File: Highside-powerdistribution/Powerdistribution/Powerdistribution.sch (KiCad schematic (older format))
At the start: 9 parts, among them J1 Screw_Terminal_01x02, J2 Screw_Terminal_01x02, J3 Screw_Terminal_01x02, J4 Screw_Terminal_01x02, J5 Screw_Terminal_01x02, J6 Screw_Terminal_01x02, J7 Screw_Terminal_01x02, J8 Screw_Terminal_01x02, J9 Screw_Terminal_01x02

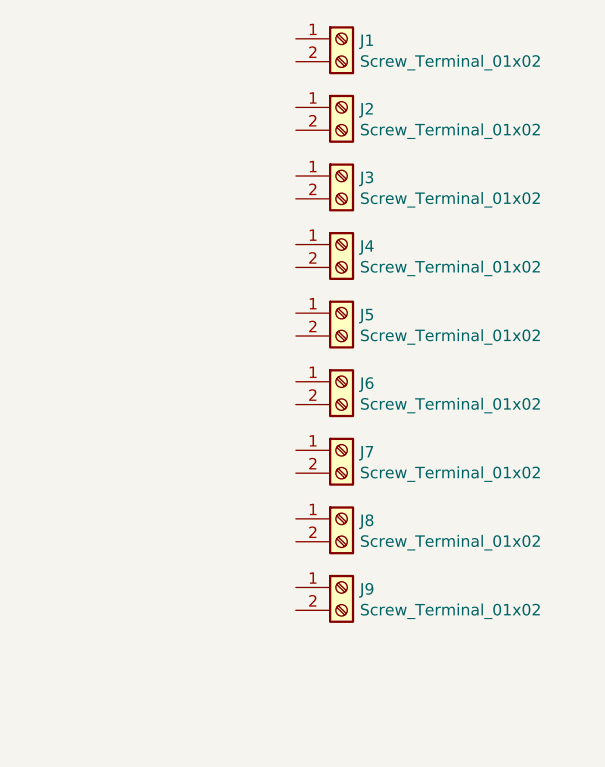
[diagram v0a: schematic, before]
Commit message: Moved filled zone to remove shortcurcit
12V and the mosfets had filled zone together
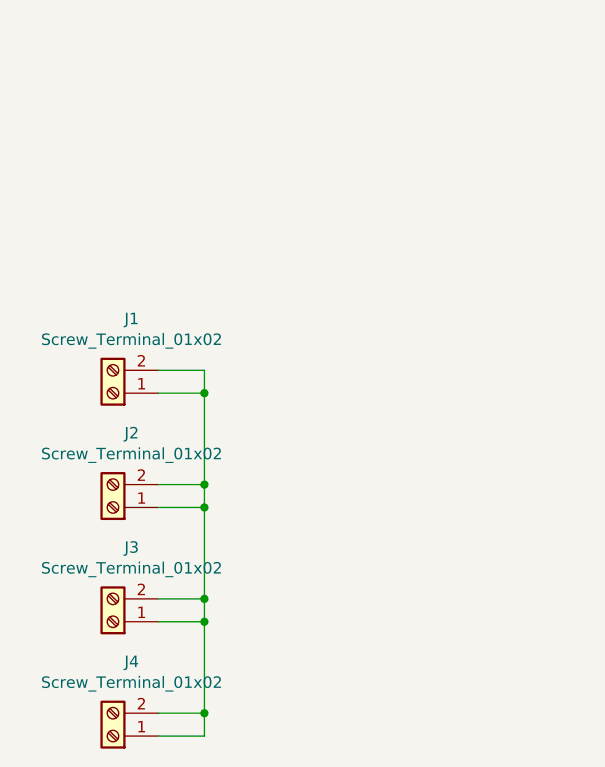
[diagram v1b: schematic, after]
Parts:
- removed J5, J6, J7, J8, J9: Screw_Terminal_01x02, TerminalBlock_TE-Connectivity:TerminalBlock_TE_282834-2_1x02_P2.54mm_Horizontal, symbol Connector:Screw_Terminal_01x02
- J1, J2, J3, J4: footprint TerminalBlock_TE-Connectivity:TerminalBlock_TE_282834-2_1x02_P2.54mm_Horizontal -> Highside-powerdistribution:Phoenix_TB_2-1935776
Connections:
- net at J1.1 (Pin_1): now also J1.2 (Pin_2), J2.1 (Pin_1), J2.2 (Pin_2), J3.1 (Pin_1), J3.2 (Pin_2), J4.1 (Pin_1), J4.2 (Pin_2)
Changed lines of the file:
@@
 EESchema Schematic File Version 4
+LIBS:Powerdistribution-cache
 EELAYER 30 0
 EELAYER END
@@
 $Comp
 L Connector:Screw_Terminal_01x02 J1
-U 1 1 5DD2F273
-P 6000 2000
-F 0 "J1" H 6080 1992 50  0000 L CNN
-F 1 "Screw_Terminal_01x02" H 6080 1901 50  0000 L CNN
-F 2 "TerminalBlock_TE-Connectivity:TerminalBlock_TE_282834-2_1x02_P2.54mm_Horizontal" H 6000 2000 50  0001 C CNN
-F 3 "~" H 6000 2000 50  0001 C CNN
-	1    6000 2000
-	1    0    0    -1
+U 1 1 5DDAC855
+P 5000 3550
+F 0 "J1" H 4918 3225 50  0000 C CNN
+F 1 "Screw_Terminal_01x02" H 4918 3316 50  0000 C CNN
+F 2 "Highside-powerdistribution:Phoenix_TB_2-1935776" H 5000 3550 50  0001 C CNN
+F 3 "~" H 5000 3550 50  0001 C CNN
+	1    5000 3550
+	-1   0    0    1
 $EndComp
+Wire Wire Line
+	5200 3450 5400 3450
 $Comp
 L Connector:Screw_Terminal_01x02 J2
-U 1 1 5DD30E21
-P 6000 2300
-F 0 "J2" H 6080 2292 50  0000 L CNN
-F 1 "Screw_Terminal_01x02" H 6080 2201 50  0000 L CNN
-F 2 "TerminalBlock_TE-Connectivity:TerminalBlock_TE_282834-2_1x02_P2.54mm_Horizontal" H 6000 2300 50  0001 C CNN
-F 3 "~" H 6000 2300 50  0001 C CNN
-	1    6000 2300
-	1    0    0    -1
+U 1 1 5E3AA3AE
+P 5000 4050
+F 0 "J2" H 4918 3725 50  0000 C CNN
+F 1 "Screw_Terminal_01x02" H 4918 3816 50  0000 C CNN
+F 2 "Highside-powerdistribution:Phoenix_TB_2-1935776" H 5000 4050 50  0001 C CNN
+F 3 "~" H 5000 4050 50  0001 C CNN
+	1    5000 4050
+	-1   0    0    1
 $EndComp
 $Comp
 L Connector:Screw_Terminal_01x02 J3
-U 1 1 5DD31107
-P 6000 2600
-F 0 "J3" H 6080 2592 50  0000 L CNN
-F 1 "Screw_Terminal_01x02" H 6080 2501 50  0000 L CNN
-F 2 "TerminalBlock_TE-Connectivity:TerminalBlock_TE_282834-2_1x02_P2.54mm_Horizontal" H 6000 2600 50  0001 C CNN
-F 3 "~" H 6000 2600 50  0001 C CNN
-	1    6000 2600
-	1    0    0    -1
+U 1 1 5E3AA843
+P 5000 4550
+F 0 "J3" H 4918 4225 50  0000 C CNN
+F 1 "Screw_Terminal_01x02" H 4918 4316 50  0000 C CNN
+F 2 "Highside-powerdistribution:Phoenix_TB_2-1935776" H 5000 4550 50  0001 C CNN
+F 3 "~" H 5000 4550 50  0001 C CNN
+	1    5000 4550
+	-1   0    0    1
 $EndComp
 $Comp
 L Connector:Screw_Terminal_01x02 J4
-U 1 1 5DD329AD
-P 6000 2900
-F 0 "J4" H 6080 2892 50  0000 L CNN
-F 1 "Screw_Terminal_01x02" H 6080 2801 50  0000 L CNN
-F 2 "TerminalBlock_TE-Connectivity:TerminalBlock_TE_282834-2_1x02_P2.54mm_Horizontal" H 6000 2900 50  0001 C CNN
-F 3 "~" H 6000 2900 50  0001 C CNN
-	1    6000 2900
-	1    0    0    -1
+U 1 1 5E3AAB69
+P 5000 5050
+F 0 "J4" H 4918 4725 50  0000 C CNN
+F 1 "Screw_Terminal_01x02" H 4918 4816 50  0000 C CNN
+F 2 "Highside-powerdistribution:Phoenix_TB_2-1935776" H 5000 5050 50  0001 C CNN
+F 3 "~" H 5000 5050 50  0001 C CNN
+	1    5000 5050
+	-1   0    0    1
 $EndComp
-$Comp
-L Connector:Screw_Terminal_01x02 J5
-U 1 1 5DD32AC5
-P 6000 3200
-F 0 "J5" H 6080 3192 50  0000 L CNN
-F 1 "Screw_Terminal_01x02" H 6080 3101 50  0000 L CNN
-F 2 "TerminalBlock_TE-Connectivity:TerminalBlock_TE_282834-2_1x02_P2.54mm_Horizontal" H 6000 3200 50  0001 C CNN
-F 3 "~" H 6000 3200 50  0001 C CNN
-	1    6000 3200
-	1    0    0    -1
-$EndComp
-$Comp
-L Connector:Screw_Terminal_01x02 J6
-U 1 1 5DD32BD8
-P 6000 3500
-F 0 "J6" H 6080 3492 50  0000 L CNN
-F 1 "Screw_Terminal_01x02" H 6080 3401 50  0000 L CNN
-F 2 "TerminalBlock_TE-Connectivity:TerminalBlock_TE_282834-2_1x02_P2.54mm_Horizontal" H 6000 3500 50  0001 C CNN
-F 3 "~" H 6000 3500 50  0001 C CNN
-	1    6000 3500
-	1    0    0    -1
-$EndComp
-$Comp
-L Connector:Screw_Terminal_01x02 J7
-U 1 1 5DD32CEB
-P 6000 3800
-F 0 "J7" H 6080 3792 50  0000 L CNN
-F 1 "Screw_Terminal_01x02" H 6080 3701 50  0000 L CNN
-F 2 "TerminalBlock_TE-Connectivity:TerminalBlock_TE_282834-2_1x02_P2.54mm_Horizontal" H 6000 3800 50  0001 C CNN
-F 3 "~" H 6000 3800 50  0001 C CNN
-	1    6000 3800
-	1    0    0    -1
-$EndComp
-$Comp
-L Connector:Screw_Terminal_01x02 J8
-U 1 1 5DD32DFE
-P 6000 4100
-F 0 "J8" H 6080 4092 50  0000 L CNN
-F 1 "Screw_Terminal_01x02" H 6080 4001 50  0000 L CNN
-F 2 "TerminalBlock_TE-Connectivity:TerminalBlock_TE_282834-2_1x02_P2.54mm_Horizontal" H 6000 4100 50  0001 C CNN
-F 3 "~" H 6000 4100 50  0001 C CNN
-	1    6000 4100
-	1    0    0    -1
-$EndComp
-$Comp
-L Connector:Screw_Terminal_01x02 J9
-U 1 1 5DD32F11
-P 6000 4400
-F 0 "J9" H 6080 4392 50  0000 L CNN
-F 1 "Screw_Terminal_01x02" H 6080 4301 50  0000 L CNN
-F 2 "TerminalBlock_TE-Connectivity:TerminalBlock_TE_282834-2_1x02_P2.54mm_Horizontal" H 6000 4400 50  0001 C CNN
-F 3 "~" H 6000 4400 50  0001 C CNN
-	1    6000 4400
-	1    0    0    -1
-$EndComp
+Wire Wire Line
+	5400 3450 5400 3550
+Wire Wire Line
+	5400 5050 5200 5050
+Wire Wire Line
+	5200 4950 5400 4950
+Connection ~ 5400 4950
+Wire Wire Line
+	5400 4950 5400 5050
+Wire Wire Line
+	5200 4550 5400 4550
+Connection ~ 5400 4550
+Wire Wire Line
+	5400 4550 5400 4950
+Wire Wire Line
+	5200 4450 5400 4450
+Connection ~ 5400 4450
+Wire Wire Line
+	5400 4450 5400 4550
+Wire Wire Line
+	5200 4050 5400 4050
+Connection ~ 5400 4050
+Wire Wire Line
+	5400 4050 5400 4450
+Wire Wire Line
+	5200 3950 5400 3950
+Connection ~ 5400 3950
+Wire Wire Line
+	5400 3950 5400 4050
+Wire Wire Line
+	5200 3550 5400 3550
+Connection ~ 5400 3550
+Wire Wire Line
+	5400 3550 5400 3950
 $EndSCHEMATC
